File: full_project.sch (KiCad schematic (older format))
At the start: 32 parts, among them J11 Conn_01x02, J12 V_OFFSET, J14 Conn_01x02, J2 Raspberry_Pi_2_3, J3 Conn_01x05_Titrator, J4 Screw_Terminal_01x04_titrator, J5 RF_Shield_Two_Pieces, J6 BNC_Jack, J7 Conn_01x02, J9 Conn_01x02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

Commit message: Added LCD and Keypad connectors, switched PSU connector to screw terminal, updated footprints, and added datasheets to parts.
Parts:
- removed J11, J9: Conn_01x02, Connector_PinSocket_2.54mm:PinSocket_1x02_P2.54mm_Vertical, symbol Connector_Generic:Conn_01x02
- removed J3: Conn_01x05_Titrator, Connector_PinSocket_2.54mm:PinSocket_1x05_P2.54mm_Vertical, symbol titrator:Conn_01x05_Titrator
- added A1: Arduino_Nano_v3.x, Module:Arduino_Nano, symbol MCU_Module:Arduino_Nano_v3.x
- added J1: Conn_01x12, Connector_PinSocket_2.54mm:PinSocket_1x12_P2.54mm_Vertical, symbol Connector_Generic:Conn_01x12
- added J3: Conn_01x08, Connector_PinSocket_2.54mm:PinSocket_1x08_P2.54mm_Vertical, symbol Connector_Generic:Conn_01x08
- added J8: Screw_Terminal_01x03, TerminalBlock:TerminalBlock_bornier-3_P5.08mm, symbol Connector:Screw_Terminal_01x03
- added RV1: R_POT, Potentiometer_THT:Potentiometer_Piher_PT-6-V_Vertical, symbol Device:R_POT
- C1: value .1uF -> 0.1uF
- C4: value 0.1uF -> .1uF
- J5: footprint RF_Shielding:Laird_Technologies_BMI-S-209-F_29.36x18.50mm -> Titrator_Footprints:44-CBSA-1.0X1.5X0.4
- U8: footprint L7805:78XXS -> Titrator_Footprints:78XXS
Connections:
- net labels added: KeyCol_1, KeyCol_2, KeyCol_3, KeyCol_4, KeyRow_1, KeyRow_2, KeyRow_3, KeyRow_4, LCD_D4, LCD_D5, LCD_D6, LCD_D7, LCD_E, LCD_OV, LCD_RS, PSU_A5V, PSU_AGND, PSU_GND
- net labels removed: *EN, PSU_12VGND, PSU_5VGND
- wire segments 176 -> 188
- no-connect marks 33 -> 42
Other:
- note added: "E"
- note added: "K"
- note added: "Keypad GPIO"
- note added: "LCD Blacklight\nAdjustment"
- note added: "VSS"
- moved on the sheet: C5, D1, J14, J7, Q1, R3

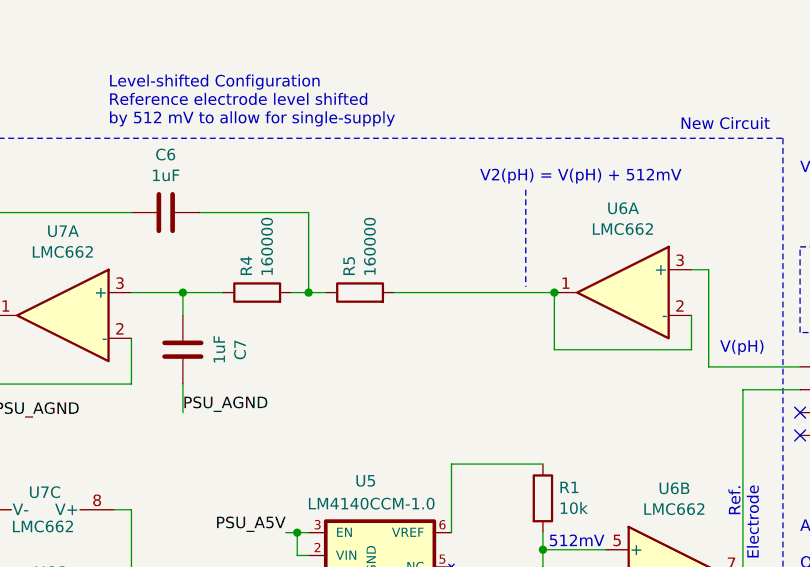
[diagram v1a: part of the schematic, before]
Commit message: added low pass filter fix on schematic and pcb
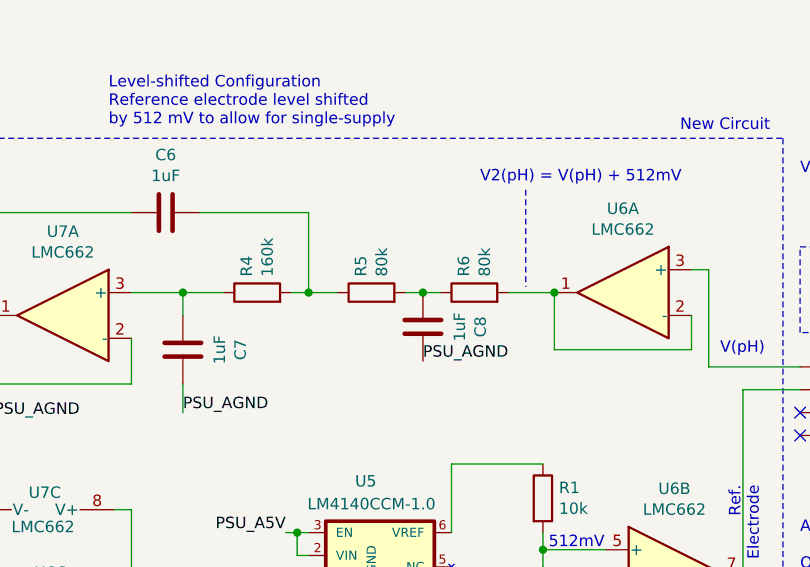
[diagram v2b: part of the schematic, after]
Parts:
- added C8: 1uF, Capacitor_THT:C_Disc_D3.8mm_W2.6mm_P2.50mm, symbol Device:C
- added R6: 80k, Resistor_THT:R_Axial_DIN0207_L6.3mm_D2.5mm_P7.62mm_Horizontal, symbol Device:R
- R4: value 160000 -> 160k
- R5: value 160000 -> 80k
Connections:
- net PSU_AGND: now also C8.2
- net at U6.1, U6.2 (-): now also R6.2; no longer R5.2
- new net: C8.1, R5.2, R6.1
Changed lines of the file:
@@
 Text Notes 7850 1900 0    50   ~ 0
 V2(pH) = V(pH) + 512mV
-$Comp
-L Device:R R5
-U 1 1 602999CE
-P 7325 2375
-F 0 "R5" H 7395 2421 50  0000 L CNN
-F 1 "160000" H 7395 2330 50  0000 L CNN
-F 2 "Resistor_THT:R_Axial_DIN0207_L6.3mm_D2.5mm_P7.62mm_Horizontal" V 7255 2375 50  0001 C CNN
-F 3 "~" H 7325 2375 50  0001 C CNN
-	1    7325 2375
-	0    -1   -1   0
-$EndComp
 Wire Wire Line
 	8850 2275 8775 2275
@@
 P 6875 2375
 F 0 "R4" H 6945 2421 50  0000 L CNN
-F 1 "160000" H 6945 2330 50  0000 L CNN
+F 1 "160k" H 6945 2330 50  0000 L CNN
 F 2 "Resistor_THT:R_Axial_DIN0207_L6.3mm_D2.5mm_P7.62mm_Horizontal" V 6805 2375 50  0001 C CNN
 F 3 "~" H 6875 2375 50  0001 C CNN
@@
 Wire Wire Line
 	7025 2375 7100 2375
-Connection ~ 7100 2375
-Wire Wire Line
-	7100 2375 7175 2375
-Wire Wire Line
-	7475 2375 8175 2375
-Connection ~ 8175 2375
 Wire Notes Line
 	9175 1700 9175 3875
@@
 Text Notes 3000 6900 0    50   ~ 0
 LCD Blacklight\nAdjustment
+$Comp
+L Device:R R5
+U 1 1 603E3A5D
+P 7375 2375
+F 0 "R5" H 7445 2421 50  0000 L CNN
+F 1 "80k" H 7445 2330 50  0000 L CNN
+F 2 "Resistor_THT:R_Axial_DIN0207_L6.3mm_D2.5mm_P7.62mm_Horizontal" V 7305 2375 50  0001 C CNN
+F 3 "~" H 7375 2375 50  0001 C CNN
+	1    7375 2375
+	0    -1   -1   0
+$EndComp
+$Comp
+L Device:R R6
+U 1 1 603E52A7
+P 7825 2375
+F 0 "R6" H 7895 2421 50  0000 L CNN
+F 1 "80k" H 7895 2330 50  0000 L CNN
+F 2 "Resistor_THT:R_Axial_DIN0207_L6.3mm_D2.5mm_P7.62mm_Horizontal" V 7755 2375 50  0001 C CNN
+F 3 "~" H 7825 2375 50  0001 C CNN
+	1    7825 2375
+	0    -1   -1   0
+$EndComp
+$Comp
+L Device:C C8
+U 1 1 603E5A82
+P 7600 2525
+F 0 "C8" V 7852 2525 50  0000 C CNN
+F 1 "1uF" V 7761 2525 50  0000 C CNN
+F 2 "Capacitor_THT:C_Disc_D3.8mm_W2.6mm_P2.50mm" H 7638 2375 50  0001 C CNN
+F 3 "~" H 7600 2525 50  0001 C CNN
+	1    7600 2525
+	1    0    0    -1
+$EndComp
+Text Label 7600 2675 0    50   ~ 0
+PSU_AGND
+Wire Wire Line
+	8175 2375 7975 2375
+Connection ~ 8175 2375
+Wire Wire Line
+	7675 2375 7600 2375
+Wire Wire Line
+	7600 2375 7525 2375
+Connection ~ 7600 2375
+Wire Wire Line
+	7225 2375 7100 2375
+Connection ~ 7100 2375
 $EndSCHEMATC

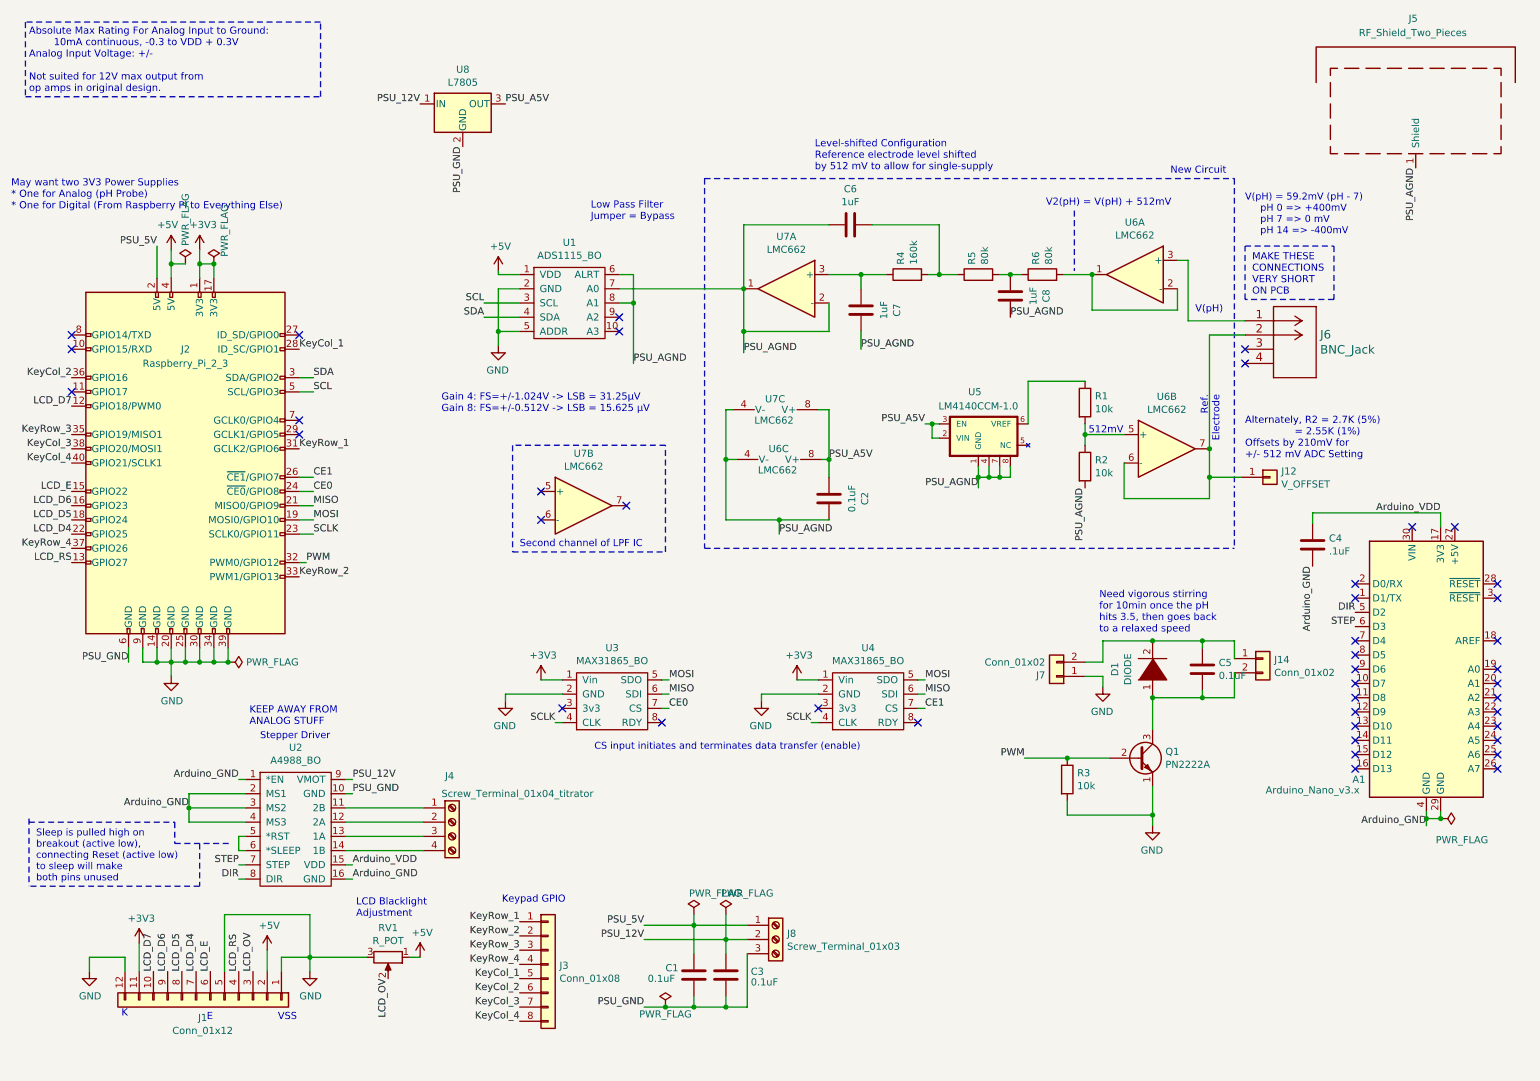
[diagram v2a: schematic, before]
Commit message: Changed connectors and made a few small updates. Changed series voltage reference to shunt
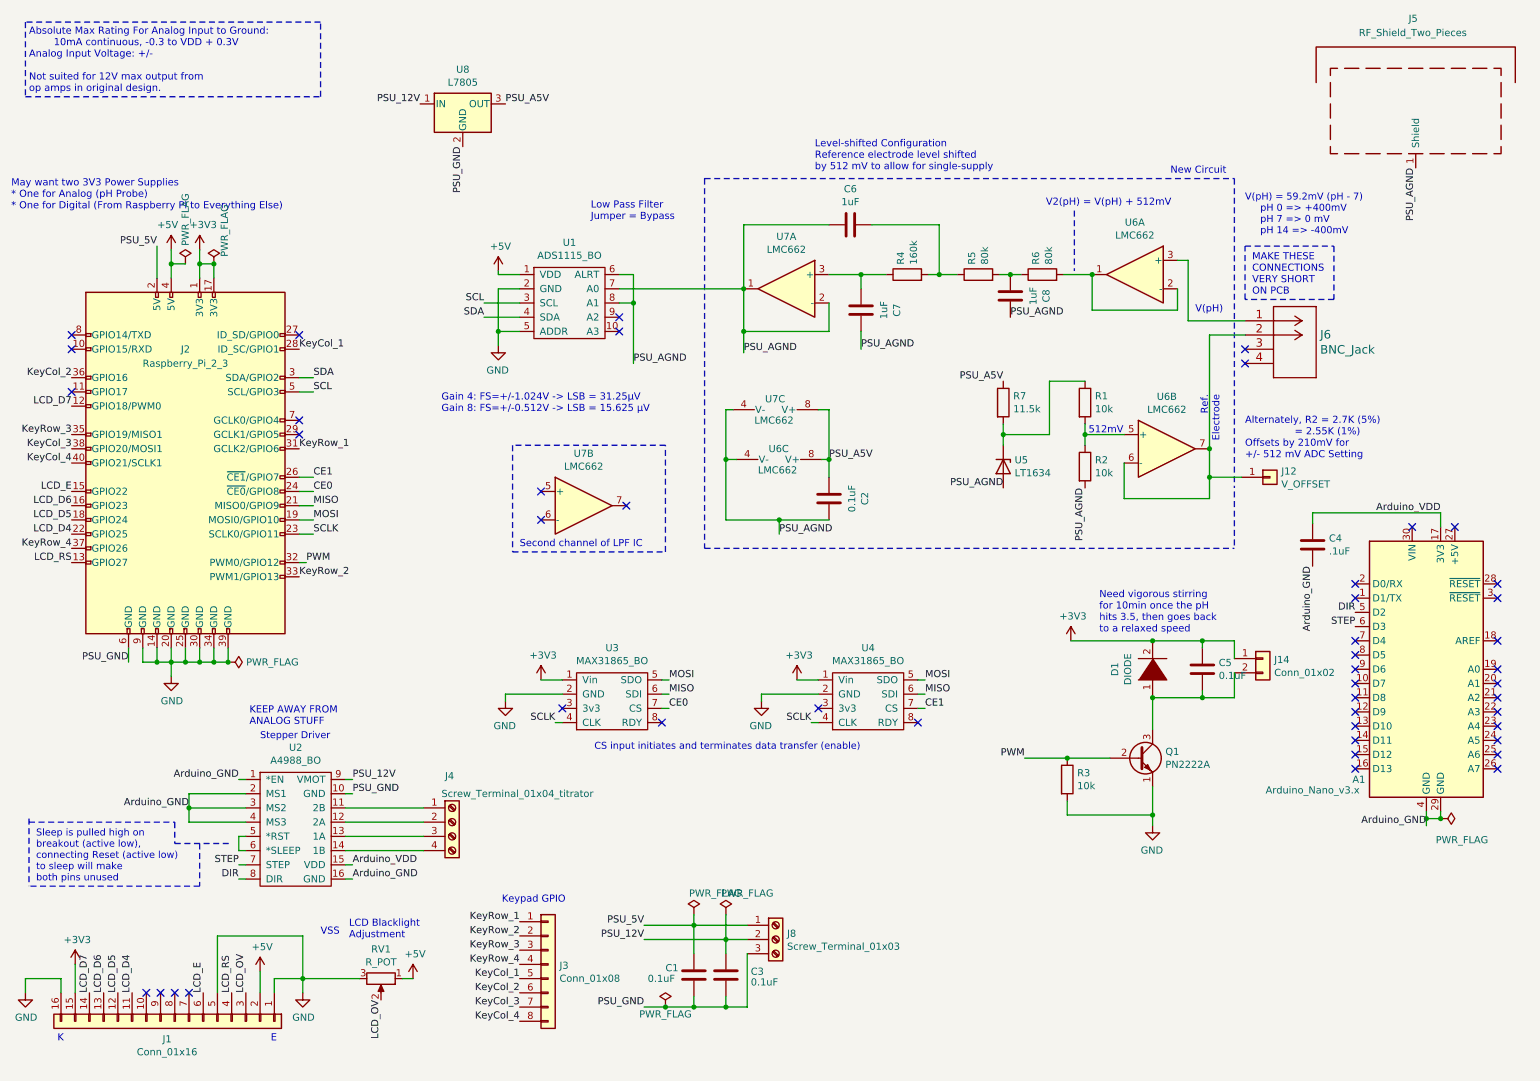
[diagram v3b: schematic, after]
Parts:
- removed J1: Conn_01x12, Connector_PinSocket_2.54mm:PinSocket_1x12_P2.54mm_Vertical, symbol Connector_Generic:Conn_01x12
- removed J7: Conn_01x02, Connector_PinSocket_2.54mm:PinSocket_1x02_P2.54mm_Vertical, symbol Connector_Generic:Conn_01x02
- removed U5: LM4140CCM-1.0, Titrator_Footprints:SOIC127P599X175-8N, symbol LM4140CCM-1.0:LM4140CCM-1.0
- added J1: Conn_01x16, Connector_Molex:Molex_SL_171971-0016_1x16_P2.54mm_Vertical, symbol Connector_Generic:Conn_01x16
- added R7: 11.5k, Resistor_THT:R_Axial_DIN0207_L6.3mm_D2.5mm_P7.62mm_Horizontal, symbol Device:R
- added U5: LT1634, Package_TO_SOT_THT:TO-92_Inline, symbol titrator:LT1634
- J3: footprint Connector_PinSocket_2.54mm:PinSocket_1x08_P2.54mm_Vertical -> Connector_Molex:Molex_SL_171971-0008_1x08_P2.54mm_Vertical
- U3, U4: footprint Titrator_Footprints:MAX31865_BO_Footprint -> Connector_Molex:Molex_SL_171971-0008_1x08_P2.54mm_Vertical
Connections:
- net +3V3: now also C5.1, D1.2 (A), J14.1 (Pin_1), J1.15 (Pin_15)
- net +5V: now also J1.2 (Pin_2)
- net GND: now also J1.1 (Pin_1), J1.16 (Pin_16), J1.5 (Pin_5)
- net LCD_D4: now also J1.11 (Pin_11)
- net LCD_D5: now also J1.12 (Pin_12)
- net LCD_D6: now also J1.13 (Pin_13)
- net LCD_D7: now also J1.14 (Pin_14)
- net LCD_E: now also J1.6 (Pin_6)
- net LCD_OV: now also J1.3 (Pin_3)
- net LCD_RS: now also J1.4 (Pin_4)
- net PSU_A5V: now also R7.1
- net PSU_AGND: now also U5.1 (A)
- net at R1.1: now also R7.2, U5.2 (K)
- no-connect marks 42 -> 46
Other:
- moved on the sheet: RV1

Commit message: help
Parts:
- J1: footprint Connector_Molex:Molex_SL_171971-0016_1x16_P2.54mm_Vertical -> Connector_PinSocket_2.54mm:PinSocket_1x16_P2.54mm_Horizontal
- J3: footprint Connector_Molex:Molex_SL_171971-0008_1x08_P2.54mm_Vertical -> Connector_PinSocket_2.54mm:PinSocket_1x08_P2.54mm_Horizontal
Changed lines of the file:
@@
 F 0 "J3" H 4430 7217 50  0000 L CNN
 F 1 "Conn_01x08" H 4430 7126 50  0000 L CNN
-F 2 "Connector_Molex:Molex_SL_171971-0008_1x08_P2.54mm_Vertical" H 4350 7225 50  0001 C CNN
+F 2 "Connector_PinSocket_2.54mm:PinSocket_1x08_P2.54mm_Horizontal" H 4350 7225 50  0001 C CNN
 F 3 "~" H 4350 7225 50  0001 C CNN
 	1    4350 7225
@@
 F 0 "J1" V 1850 7571 50  0000 C CNN
 F 1 "Conn_01x16" V 1941 7571 50  0000 C CNN
-F 2 "Connector_Molex:Molex_SL_171971-0016_1x16_P2.54mm_Vertical" H 1725 7625 50  0001 C CNN
+F 2 "Connector_PinSocket_2.54mm:PinSocket_1x16_P2.54mm_Horizontal" H 1725 7625 50  0001 C CNN
 F 3 "~" H 1725 7625 50  0001 C CNN
 	1    1725 7625

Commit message: Switched GPIO on rasp. π for better routing, added in all 3d models
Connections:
- net KeyCol_1: now also J2.36 (GPIO16); no longer J2.28 (ID_SC/GPIO1)
- net KeyCol_2: now also J2.37 (GPIO26); no longer J2.36 (GPIO16)
- net KeyRow_1: now also J2.28 (ID_SC/GPIO1); no longer J2.31 (GCLK2/GPIO6)
- net KeyRow_2: now also J2.31 (GCLK2/GPIO6); no longer J2.33 (PWM1/GPIO13)
- net KeyRow_3: now also J2.32 (PWM0/GPIO12); no longer J2.35 (GPIO19/MISO1)
- net KeyRow_4: now also J2.35 (GPIO19/MISO1); no longer J2.37 (GPIO26)
- net LCD_D4: now also J2.12 (GPIO18/PWM0); no longer J2.22 (GPIO25)
- net LCD_D5: now also J2.16 (GPIO23); no longer J2.18 (GPIO24)
- net LCD_D6: now also J2.18 (GPIO24); no longer J2.16 (GPIO23)
- net LCD_D7: now also J2.22 (GPIO25); no longer J2.12 (GPIO18/PWM0)
- net PWM: now also J2.33 (PWM1/GPIO13); no longer J2.32 (PWM0/GPIO12)
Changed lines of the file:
@@
 Wire Wire Line
 	2650 4400 2600 4400
-Text Label 2650 4400 0    50   ~ 0
+Text Label 2600 4500 0    50   ~ 0
 PWM
 $Comp
@@
 Text Label 4150 7625 2    50   ~ 0
 KeyCol_4
-Text Label 2600 2900 0    50   ~ 0
+Text Label 1000 3100 2    50   ~ 0
 KeyCol_1
 NoConn ~ 2600 2800
-Text Label 1000 3100 2    50   ~ 0
+Text Label 1000 4300 2    50   ~ 0
 KeyCol_2
 Text Label 1000 3600 2    50   ~ 0
@@
 Text Label 1000 3700 2    50   ~ 0
 KeyCol_4
+Text Label 2600 2900 0    50   ~ 0
+KeyRow_1
 Text Label 2600 3600 0    50   ~ 0
-KeyRow_1
-Text Label 2600 4500 0    50   ~ 0
 KeyRow_2
+Text Label 2650 4400 0    50   ~ 0
+KeyRow_3
 Text Label 1000 3500 2    50   ~ 0
-KeyRow_3
-Text Label 1000 4300 2    50   ~ 0
 KeyRow_4
 Text Notes 4025 6800 0    50   ~ 0
@@
 Text Label 2225 7425 1    50   ~ 0
 LCD_OV
+Text Label 1000 4200 2    50   ~ 0
+LCD_D7
+Text Label 1000 4100 2    50   ~ 0
+LCD_D6
+Text Label 1000 4000 2    50   ~ 0
+LCD_D5
 Text Label 1000 3300 2    50   ~ 0
-LCD_D7
-Text Label 1000 4000 2    50   ~ 0
-LCD_D6
-Text Label 1000 4100 2    50   ~ 0
-LCD_D5
-Text Label 1000 4200 2    50   ~ 0
 LCD_D4
 Text Label 1000 3900 2    50   ~ 0

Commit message: I made a colander
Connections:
- net GND: now also J2.6 (GND); no longer J2.39 (GND)
- net PSU_GND: now also J2.39 (GND); no longer J2.6 (GND)
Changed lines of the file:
@@
 L power:PWR_FLAG #FLG0101
 U 1 1 5F2D3010
-P 2100 5100
-F 0 "#FLG0101" H 2100 5175 50  0001 C CNN
-F 1 "PWR_FLAG" V 2100 5227 50  0000 L CNN
-F 2 "" H 2100 5100 50  0001 C CNN
-F 3 "~" H 2100 5100 50  0001 C CNN
-	1    2100 5100
-	0    1    1    0
+P 1400 5100
+F 0 "#FLG0101" H 1400 5175 50  0001 C CNN
+F 1 "PWR_FLAG" V 1400 5227 50  0000 L CNN
+F 2 "" H 1400 5100 50  0001 C CNN
+F 3 "~" H 1400 5100 50  0001 C CNN
+	1    1400 5100
+	0    -1   -1   0
 $EndComp
 Connection ~ 1900 5100
@@
 	1900 5000 1900 5100
 Wire Wire Line
-	2000 5100 2100 5100
-Wire Wire Line
 	1900 5100 2000 5100
-Connection ~ 2000 5100
 Wire Wire Line
 	2000 5000 2000 5100
-Wire Wire Line
-	2100 5100 2100 5000
 Wire Wire Line
 	1500 5000 1500 5100
@@
 	1    0    0    -1
 $EndComp
-Connection ~ 2100 5100
-Text Label 1400 5100 2    50   ~ 0
+Text Label 2100 5000 0    50   ~ 0
 PSU_GND
 Wire Wire Line
@@
 NoConn ~ 1725 7425
 NoConn ~ 1825 7425
+Wire Wire Line
+	1400 5100 1500 5100
+Connection ~ 1400 5100
+Connection ~ 1500 5100
 $EndSCHEMATC
